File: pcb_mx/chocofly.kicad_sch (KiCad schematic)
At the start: 134 parts, among them P1 battery+, P2 battery-, SW1 SW_Push, SW11 SW_Push, SW12 SW_Push, SW13 SW_Push, SW14 SW_Push, SW15 SW_Push, SW16 SW_Push, SW17 SW_Push, SW18 SW_Push, SW19 SW_Push, SW2 SW_Push, SW20 SW_Push, SW21 SW_Push, SW22 SW_Push, SW23 SW_Push, SW24 SW_Push, SW25 SW_Push, SW26 SW_Push, SW27 SW_Push, SW28 SW_Push, SW29 SW_Push, SW3 SW_Push, SW30 SW_Push, SW31 SW_Push, SW32 SW_Push, SW33 SW_Push, SW34 SW_Push, SW35 SW_Push, SW36 SW_Push, SW37 SW_Push, SW38 SW_Push, SW39 SW_Push, SW4 SW_Push, SW40 SW_Push, SW41 SW_Push, SW42 SW_Push, SW43 SW_Push, SW44 SW_Push, SW45 SW_Push, SW46 SW_Push, SW47 SW_Push, SW48 SW_Push, SW49 SW_Push, SW5 SW_Push, SW50 SW_Push, SW51 SW_Push, SW52 SW_Push, SW53 SW_Push, SW54 SW_Push, SW55 SW_Push, SW56 SW_Push, SW57 SW_Push, SW58 SW_Push, SW59 SW_Push, SW6 SW_Push, SW60 SW_Push, SW61 SW_Push, SW62 Reset, SW63 Power, SW64 Power, SW7 SW_Push, SW8 SW_Push, SW9 SW_Push

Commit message: wip
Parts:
- ENC1, ENC2: value EVQWGD001 -> EVQWGD001_for_mx; footprint footprints:EVQWGD001 -> footprints:EVQWGD001_for_mx
- SW1, SW11, SW12, SW13, SW14, SW15, SW16, SW17, SW18, SW19, SW2, SW20, SW21, SW22, SW23, SW24, SW25, SW26, SW27, SW28, SW29, SW3, SW30, SW31, SW32, SW33, SW34, SW35, SW36, SW37, SW38, SW39, SW4, SW40, SW41, SW42, SW43, SW44, SW45, SW46, SW47, SW48, SW49, SW5, SW50, SW51, SW52, SW53, SW54, SW55, SW56, SW57, SW58, SW59, SW6, SW60, SW61, SW7, SW8, SW9: footprint footprints:Kailh_socket_PG1350_chosfox_17_5mm -> footprints:CherryMX_MidHeight_Hotswap_1u

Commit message: wip
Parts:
- removed SW64: Power, footprints:Switch_MSK-12C01-07, symbol Switch:SW_DPDT_x2
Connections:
- no-connect marks 6 -> 5
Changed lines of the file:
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@@
 	)
 	(junction
-		(at 231.14 93.98)
-		(diameter 0)
-		(color 0 0 0 0)
-	)
-	(junction
 		(at 156.21 72.39)
 		(diameter 0)
@@
 	)
 	(junction
-		(at 259.08 96.52)
-		(diameter 0)
-		(color 0 0 0 0)
-	)
-	(junction
 		(at 114.3 102.87)
 		(diameter 0)
@@
 	)
 	(no_connect
-		(at 242.57 78.74)
-	)
-	(no_connect
 		(at 128.27 34.29)
 	)
@@
 	(wire
 		(pts
-			(xy 259.08 96.52) (xy 265.43 96.52)
+			(xy 242.57 96.52) (xy 265.43 96.52)
 		)
 		(stroke
@@
 	(wire
 		(pts
-			(xy 231.14 81.28) (xy 231.14 93.98)
-		)
-		(stroke
-			(width 0)
-			(type default)
-		)
-	)
-	(wire
-		(pts
-			(xy 231.14 93.98) (xy 218.44 93.98)
-		)
-		(stroke
-			(width 0)
-			(type default)
-		)
-	)
-	(wire
-		(pts
 			(xy 132.08 110.49) (xy 146.05 110.49)
 		)
@@
 	(wire
 		(pts
-			(xy 242.57 96.52) (xy 259.08 96.52)
-		)
-		(stroke
-			(width 0)
-			(type default)
-		)
-	)
-	(wire
-		(pts
 			(xy 62.23 95.25) (xy 76.2 95.25)
 		)
@@
 	(wire
 		(pts
-			(xy 232.41 81.28) (xy 231.14 81.28)
-		)
-		(stroke
-			(width 0)
-			(type default)
-		)
-	)
-	(wire
-		(pts
 			(xy 48.26 80.01) (xy 62.23 80.01)
 		)
@@
 	(wire
 		(pts
-			(xy 242.57 83.82) (xy 259.08 83.82)
-		)
-		(stroke
-			(width 0)
-			(type default)
-		)
-	)
-	(wire
-		(pts
 			(xy 34.29 125.73) (xy 48.26 125.73)
 		)
@@
 	(wire
 		(pts
-			(xy 259.08 83.82) (xy 259.08 96.52)
-		)
-		(stroke
-			(width 0)
-			(type default)
-		)
-	)
-	(wire
-		(pts
 			(xy 62.23 21.59) (xy 68.58 21.59)
 		)
@@
 	(wire
 		(pts
-			(xy 232.41 93.98) (xy 231.14 93.98)
+			(xy 218.44 93.98) (xy 232.41 93.98)
 		)
 		(stroke
@@
 					(unit 1)
 				)
-			)
-		)
-	)
-	(symbol
-		(lib_id "Switch:SW_DPDT_x2")
-		(at 237.49 81.28 0)
-		(unit 1)
-		(exclude_from_sim no)
-		(in_bom yes)
-		(on_board yes)
-		(dnp no)
-		(property "Reference" "SW64"
-			(at 237.49 74.041 0)
-			(effects
-				(font
-					(size 1.27 1.27)
-				)
-			)
-		)
-		(property "Value" "Power"
-			(at 237.49 76.3524 0)
-			(effects
-				(font
-					(size 1.27 1.27)
-				)
-			)
-		)
-		(property "Footprint" "footprints:Switch_MSK-12C01-07"
-			(at 237.49 81.28 0)
-			(effects
-				(font
-					(size 1.27 1.27)
-				)
-				(hide yes)
-			)
-		)
-		(property "Datasheet" "~"
-			(at 237.49 81.28 0)
-			(effects
-				(font
-					(size 1.27 1.27)
-				)
-				(hide yes)
-			)
-		)
-		(property "Description" ""
-			(at 237.49 81.28 0)
-			(effects
-				(font
-					(size 1.27 1.27)
-				)
-				(hide yes)
-			)
-		)
-		(pin "1"
-		)
-		(pin "2"
-		)
-		(pin "3"
-		)
-		(pin "4"
-		)
-		(pin "5"
-		)
-		(pin "6"
-		)
-		(instances
-			(project "chocofly"
-				(path "/db4dac64-1581-426b-b2ad-fbb21197bc47"
-					(reference "SW64")
-					(unit 1)
-				)

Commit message: wip on chocomx
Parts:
- removed D10, D62: 1N4148, footprints:diode_TH_SMD, symbol Diode:1N4148
- removed ENC1, ENC2: EVQWGD001_for_mx, footprints:EVQWGD001_for_mx, symbol chocofly-rescue:EVQWGD001-evqwgd001
- removed JP1, JP2: Jumper_NC_Small, footprints:avalanche_Jumper_NC, symbol chocofly-rescue:Jumper_NC_Small-Device
- removed JP3, JP4: Jumper_NC_Small, footprints:avalanche_Jumper, symbol chocofly-rescue:Jumper_NO_Small-Device
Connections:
- net encA: no longer names the net of MCU1.1 (TX(PD3))
- net encB: no longer names the net of MCU1.2 (RX(PD2))

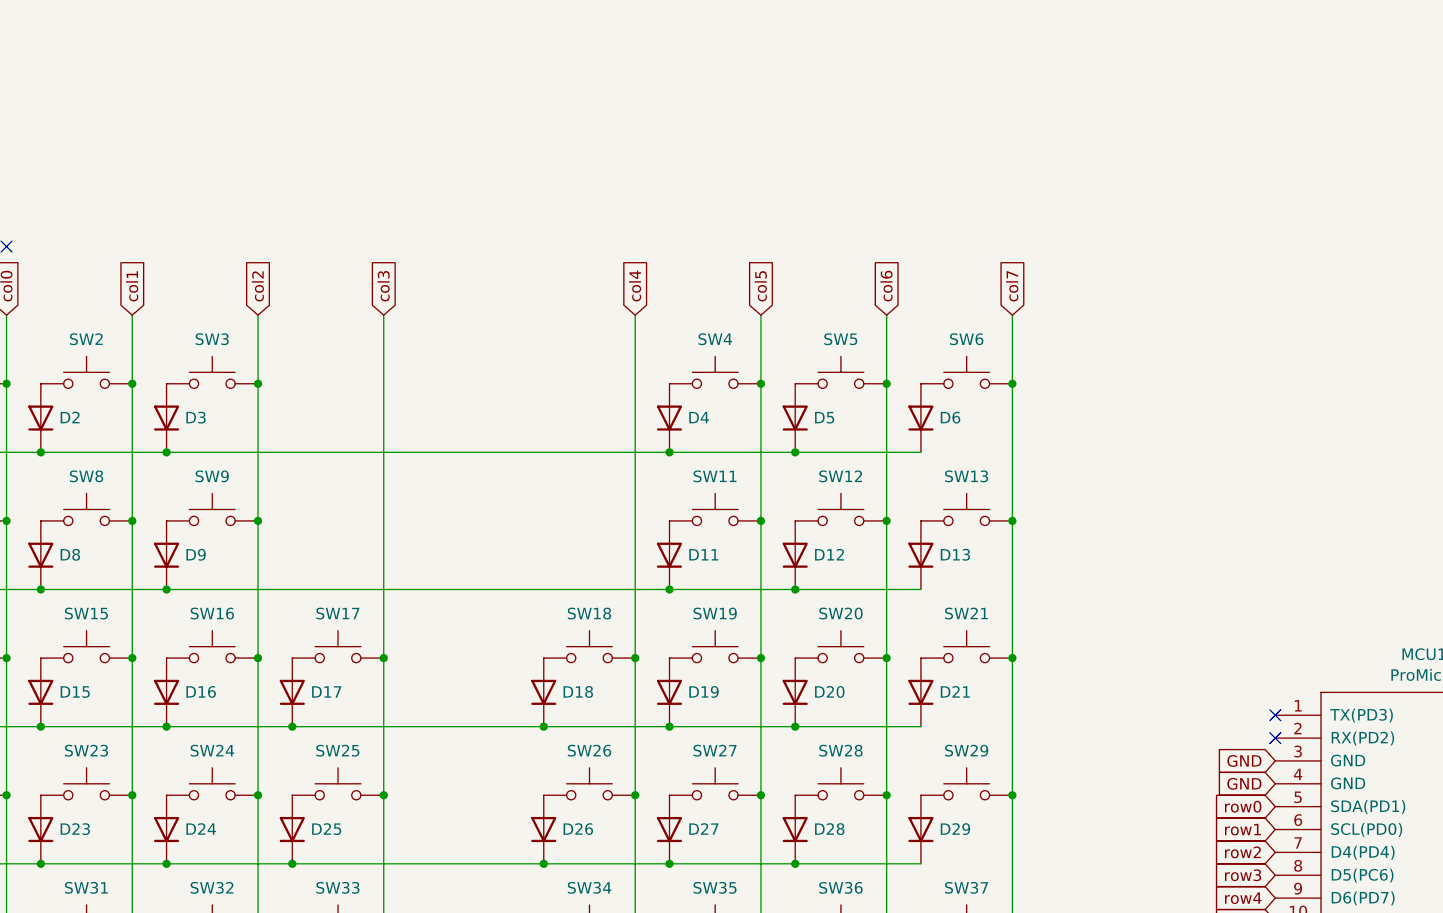
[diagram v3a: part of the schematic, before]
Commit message: added encoder back
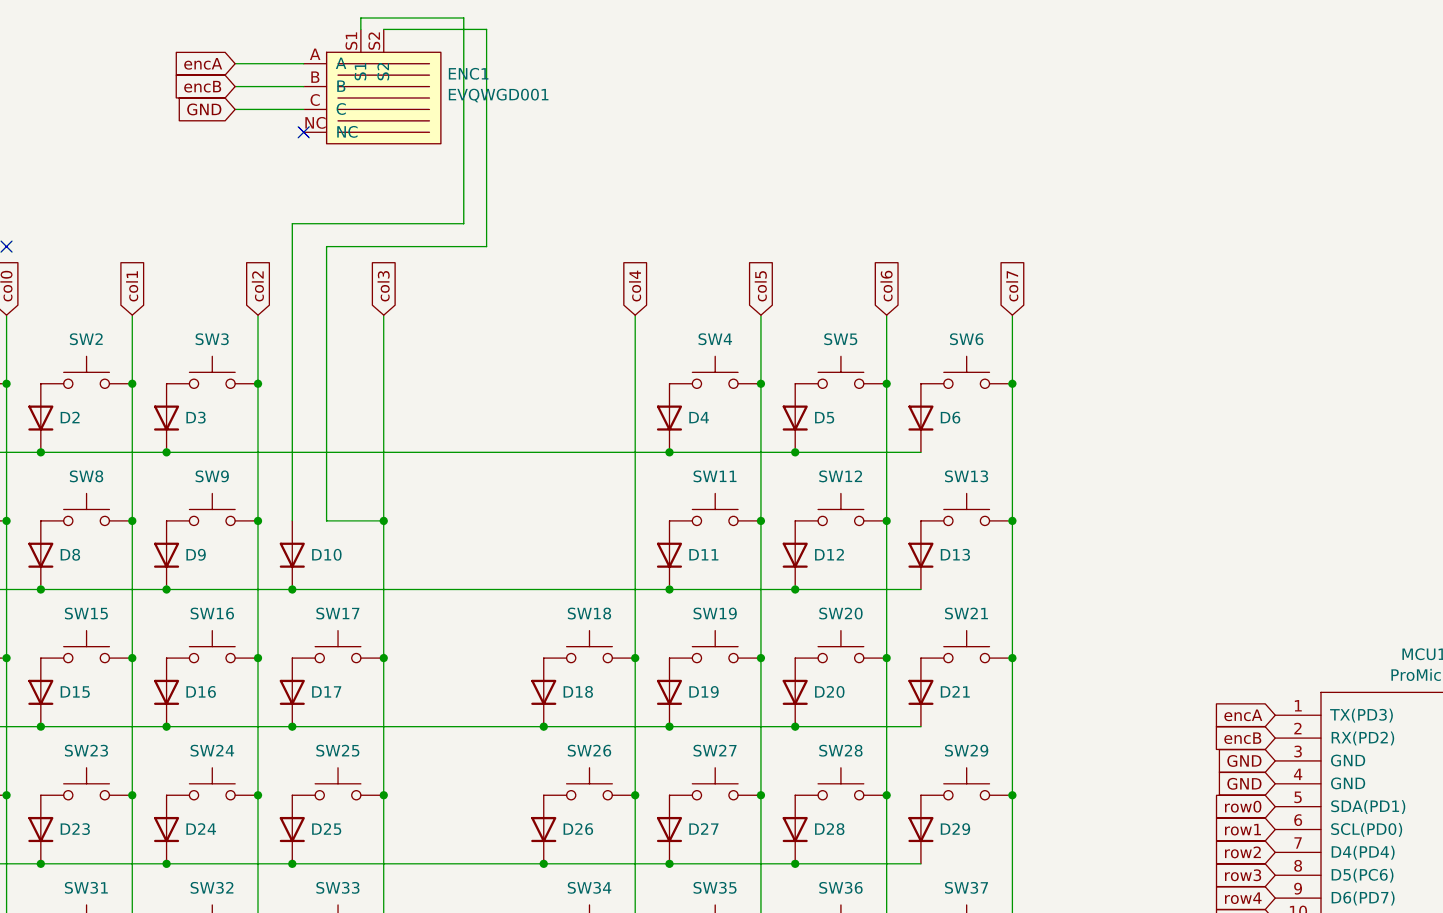
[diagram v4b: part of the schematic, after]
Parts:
- added D10: 1N4148, footprints:diode_TH_SMD, symbol Diode:1N4148
- added ENC1: EVQWGD001, footprints:EVQWGD001, symbol chocofly-rescue:EVQWGD001-evqwgd001
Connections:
- net GND: now also ENC1.C
- net col3: now also ENC1.S2
- net row1: now also D10.1 (K)
- net encA: now reaches MCU1.1 (TX(PD3))
- net encA: now also ENC1.A
- net encB: now reaches MCU1.2 (RX(PD2))
- net encB: now also ENC1.B
- new net: D10.2 (A), ENC1.S1
- no-connect marks 5 -> 4

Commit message: mounting holes added
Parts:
- added H1, H10, H11, H12, H13, H14, H15, H16, H2, H3, H4, H5, H6, H7, H8, H9: MountingHole, MountingHole:MountingHole_2.2mm_M2, symbol Mechanical:MountingHole
